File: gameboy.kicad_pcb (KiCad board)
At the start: 4 copper layers, 90 x 125 mm, 103 parts, among them J1 SM03B-SRSS-TB, J2 FPC-05F-12PH20, J3 Conn_01x02, J4 Conn_01x02, J5 Conn_01x02, J6 SD_Card_Receptacle, J7 USB_C_Receptacle_USB2.0_16P, Q1 SS8050, Q2 AO3401A, Q3 SS8050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

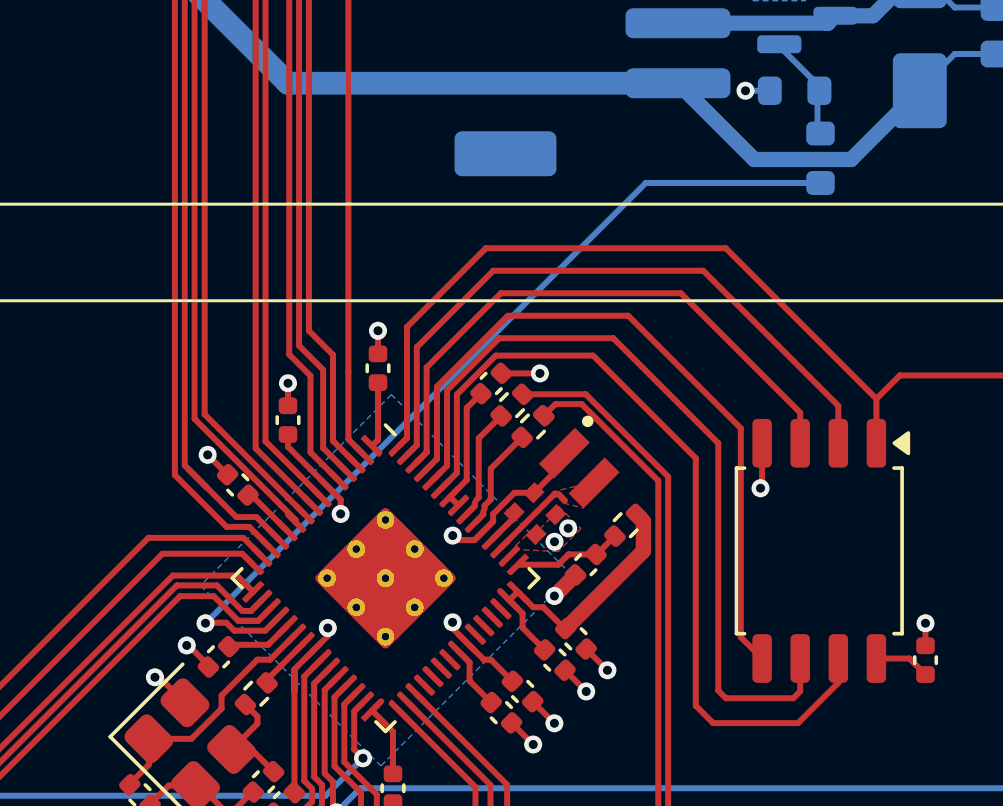
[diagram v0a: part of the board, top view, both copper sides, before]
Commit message: change trace cutting zone
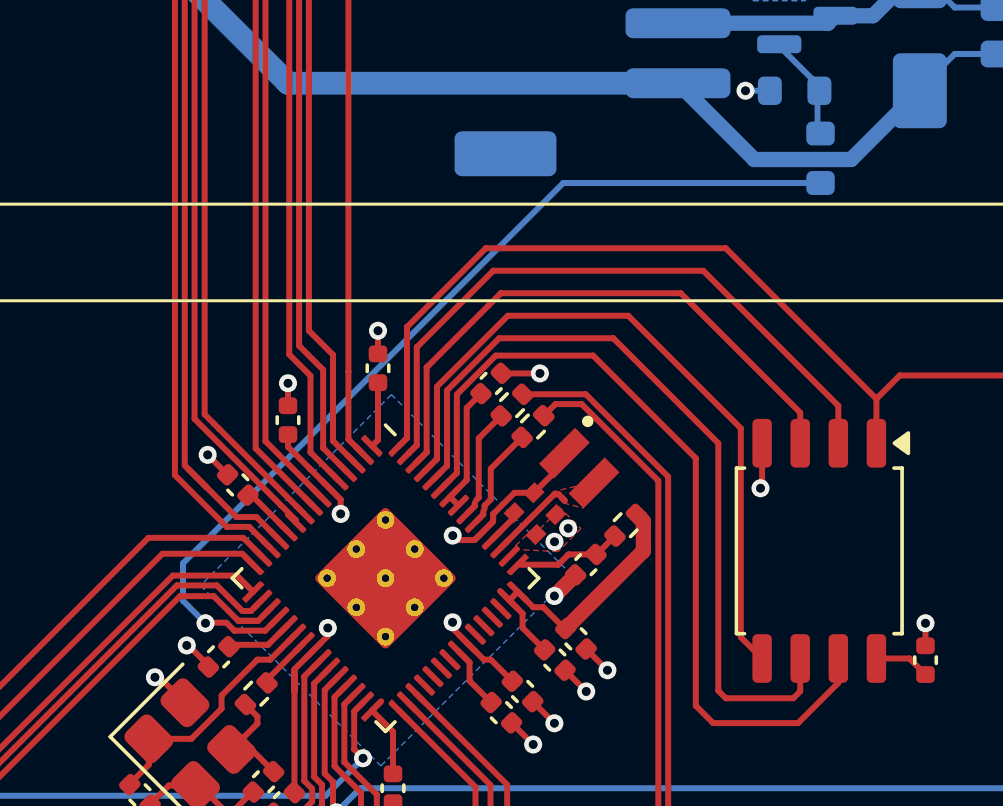
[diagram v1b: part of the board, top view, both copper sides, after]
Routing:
- net /MCU/VIB_EN: track 29.3 -> 31.6 mm

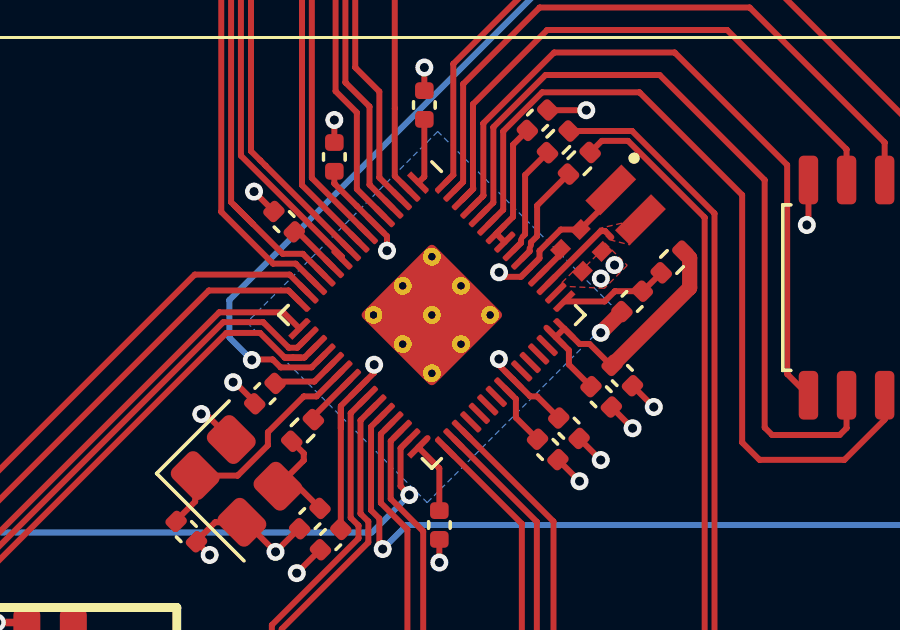
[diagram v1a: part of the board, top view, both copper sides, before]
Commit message: add lcd model
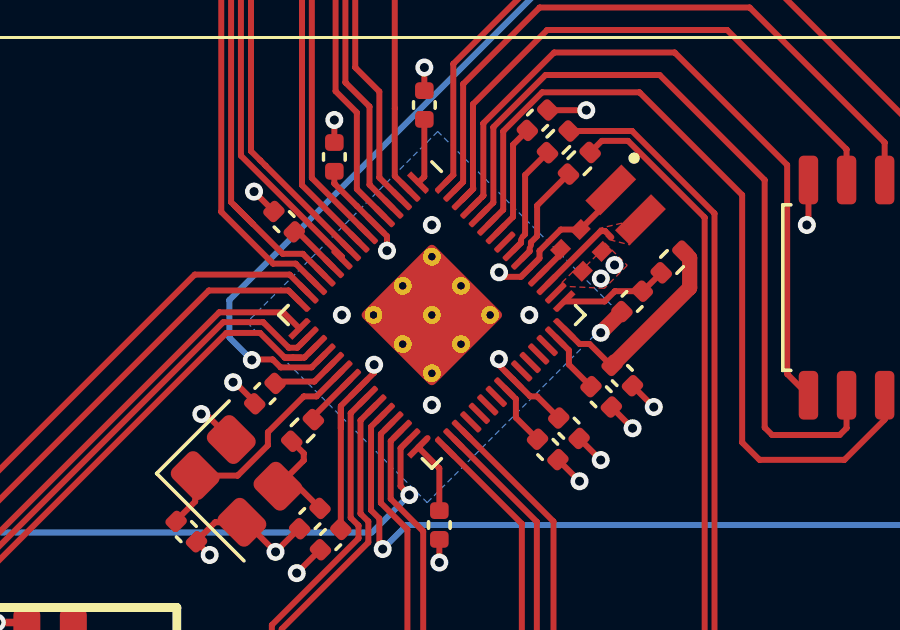
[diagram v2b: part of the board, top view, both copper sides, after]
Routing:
- net +3V3: track 67.0 -> 65.8 mm, vias 83 -> 87

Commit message: minor cleanup
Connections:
- J1 pad MP: GND -> unconnected-(J1-MountPin-PadMP)_1
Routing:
- net GND: track 147.7 -> 135.2 mm, vias 135 -> 108
- net /MCU/VIB_EN: track 31.6 -> 34.0 mm
- net /Buttons/BTN_UP: track 30.1 -> 31.8 mm
- net /MCU/SD_MISO: track 75.7 -> 75.0 mm
- net /MCU/SD_MOSI: track 76.8 -> 76.3 mm
- net /Audio/I2S_LRCLK: track 89.3 -> 88.8 mm
- net +3V3: track 65.8 -> 65.7 mm, vias 87 -> 57

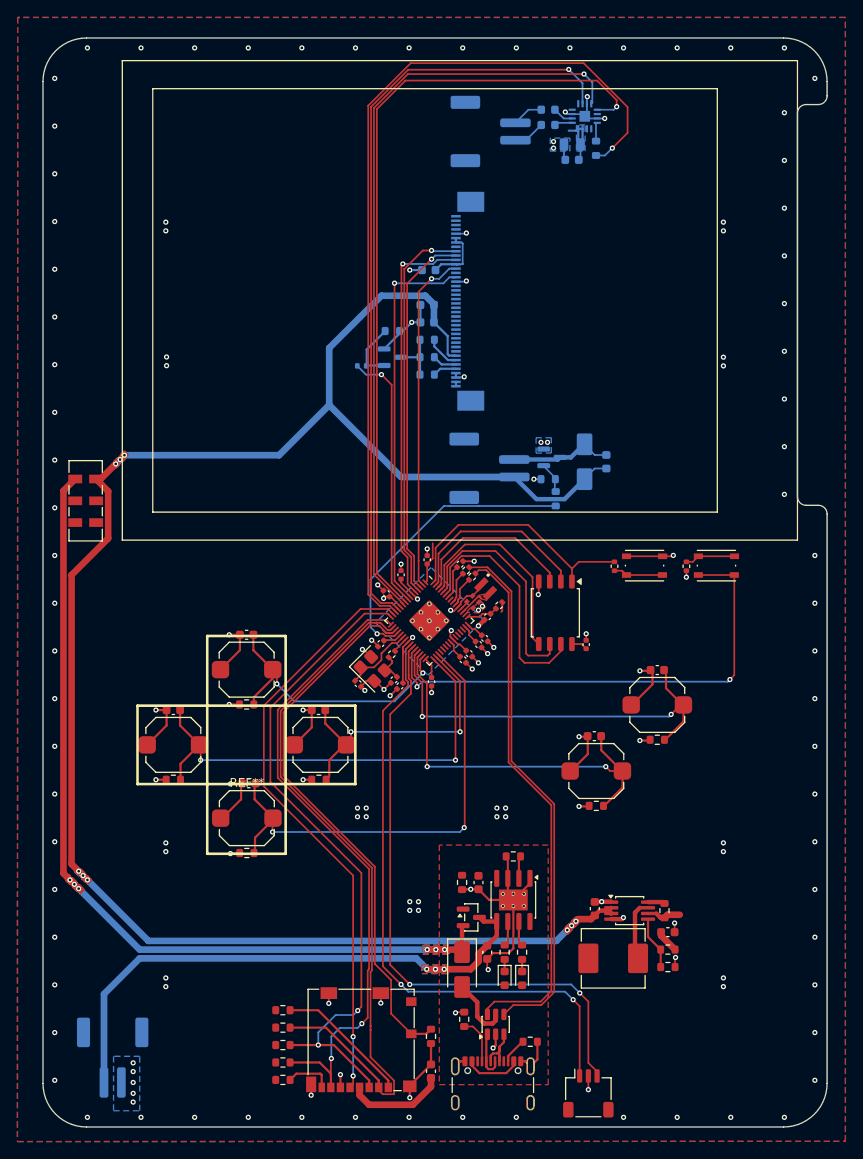
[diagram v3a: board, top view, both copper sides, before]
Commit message: add silkscreen, optimize layout and replace sd card peripheral
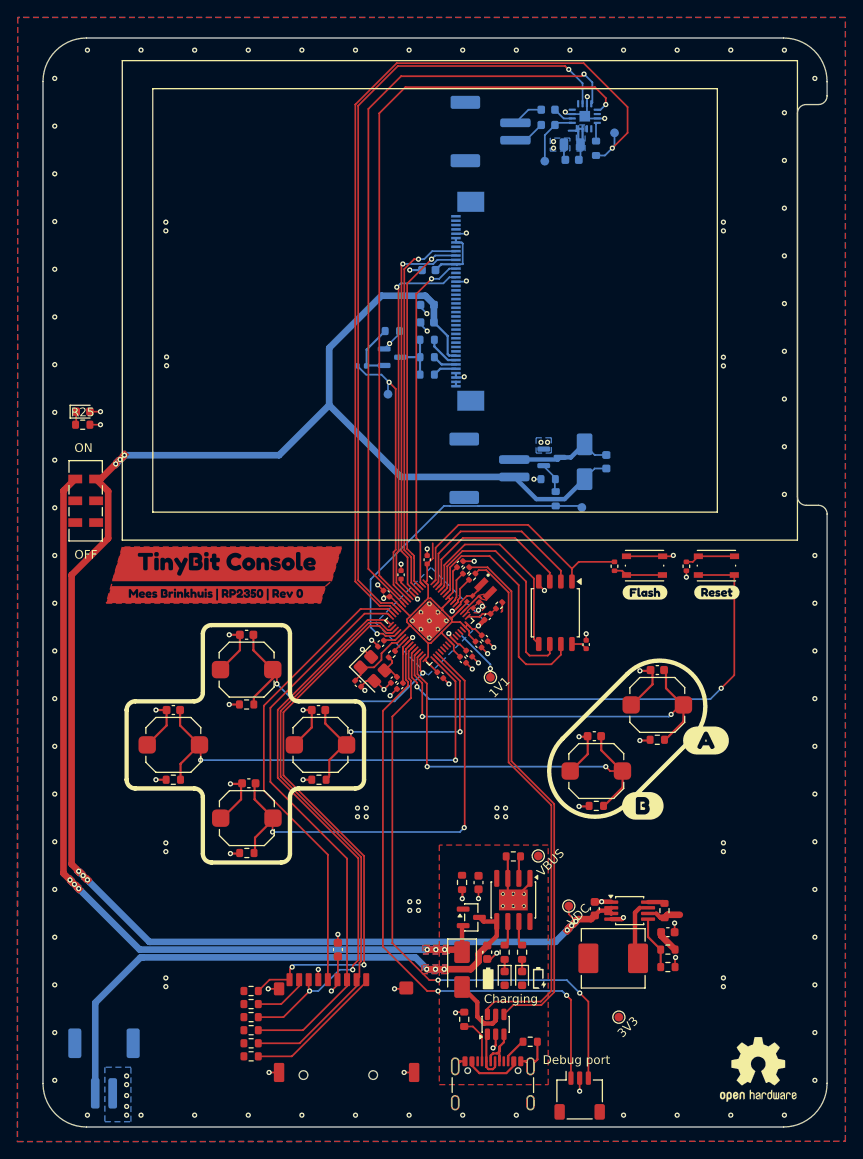
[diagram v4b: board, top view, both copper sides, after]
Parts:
- added D5: GREEN, LED_SMD:LED_0603_1608Metric, F.Cu at (103.5, 74.2)
- added G***: LOGO, icons:battery_full, F.Cu at (150.0, 139.3)
- added G***: LOGO, icons:battery_charging, F.Cu at (155.8, 139.2)
- added R25: 1k, Resistor_SMD:R_0603_1608Metric, F.Cu at (103.5, 75.8)
- added REF**: OSHW-Logo2_9.8x8mm_SilkScreen, Symbol:OSHW-Logo2_9.8x8mm_SilkScreen, F.Cu at (181.0, 149.8)
- added TP1: TestPoint, TestPoint:TestPoint_Pad_D1.0mm, F.Cu at (155.8, 125.2)
- added TP10: TestPoint, TestPoint:TestPoint_Pad_D1.0mm, F.Cu at (150.3, 104.8)
- added TP2: TestPoint, TestPoint:TestPoint_Pad_D1.0mm, F.Cu at (159.2, 131.0)
- added TP3: TestPoint, TestPoint:TestPoint_Pad_D1.0mm, F.Cu at (165.0, 143.8)
- added TP5: TestPoint, TestPoint:TestPoint_Pad_D1.0mm, B.Cu at (156.5, 45.5)
- added TP7: TestPoint, TestPoint:TestPoint_Pad_D1.0mm, B.Cu at (160.8, 85.2)
- added TP8: TestPoint, TestPoint:TestPoint_Pad_D1.0mm, B.Cu at (138.5, 72.2)
- added TP9: TestPoint, TestPoint:TestPoint_Pad_D1.0mm, B.Cu at (164.5, 42.2)
- added kibuzzard-697346E9: G***, kibuzzard-697346E9, F.Cu at (120.0, 91.8)
- added kibuzzard-6973473F: G***, kibuzzard-6973473F, F.Cu at (175.0, 112.0)
- added kibuzzard-69734758: G***, kibuzzard-69734758, F.Cu at (167.8, 119.5)
- added kibuzzard-6973477C: G***, kibuzzard-6973477C, F.Cu at (168.0, 95.0)
- added kibuzzard-69734789: G***, kibuzzard-69734789, F.Cu at (176.2, 95.0)
- added kibuzzard-69734872: G***, kibuzzard-69734872, F.Cu at (118.8, 95.2)
- J6: footprint Connector_Card:microSD_HC_Molex_104031-0811 -> RP2350_60QFN_minimal:SHOU HAN
- moved R32 21.3 mm to (122.8, 140.8), turned to 0 degrees
- moved C28 17.6 mm to (132.8, 136.0)
- moved R29 9.44 mm to (122.8, 142.2)
- moved R34 6.43 mm to (122.8, 148.2)
- moved R30 6.36 mm to (122.8, 143.7)
- moved R33 4.07 mm to (122.8, 146.8)
- moved R31 4.03 mm to (122.8, 145.2)
- moved J6 2.37 mm to (133.5, 145.0), turned to 0 degrees
- moved J3 1.60 mm to (105.9, 149.7)
- moved C12 1.25 mm to (144.5, 104.5), turned to -45 degrees
- moved J1 1.03 mm to (160.5, 152.8)
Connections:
- J6 pad 10: +3V3 -> GND
- R32 pad 1: /MCU/SD_DET -> +3V3
- R32 pad 2: GND -> /MCU/SD_DET
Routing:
- net +3V3: track 65.7 -> 88.6 mm, vias 57 -> 59
- net GND: track 135.2 -> 116.0 mm, vias 108 -> 113
- net /MCU/SD_SS: track 82.6 -> 67.3 mm
- net /MCU/SD_CLK: track 67.9 -> 54.2 mm, vias 2 -> 0
- net /MCU/SD_MOSI: track 76.3 -> 66.3 mm, vias 2 -> 0
- net /MCU/SD_MISO: track 75.0 -> 65.9 mm
- net +1V1: track 17.6 -> 23.4 mm, vias 4 -> 5
- net Net-(U5-OUTP): track 1.73 -> 6.37 mm
- net /Audio/I2S_SDMODE: track 101.6 -> 105.7 mm
- net /Audio/I2S_DIN: track 90.9 -> 87.1 mm
- net /MCU/VIB_EN: track 34.0 -> 37.1 mm
- net /Audio/I2S_LRCLK: track 88.8 -> 91.3 mm
- net VDC: track 213.6 -> 215.8 mm
- net /Power/BAT+: track 65.4 -> 67.1 mm
- net /MCU/SWCLK: track 71.0 -> 69.3 mm
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- added copper zone on F.Cu, net (none)
- removed copper zone on B.Cu, net /Power/BAT+
- removed copper zone on F.Cu, net /Power/BAT+
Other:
- board text added: "1V1"
- board text added: "3V3"
- board text added: "Backlight enabled"
- board text added: "Charging"
- board text added: "Debug port"
- board text added: "OFF"
- board text added: "ON"
- board text added: "Speaker enabled"
- board text added: "VBUS"
- board text added: "VDC"
- board text added: "Vibration enabled"
- board text added: "speaker output"
